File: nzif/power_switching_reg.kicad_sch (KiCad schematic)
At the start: 46 parts, among them U1101 LT8330xS6, U1102 ADP2303ARDZ, U1103 ADP2303ARDZ, U1104 ADP2303ARDZ

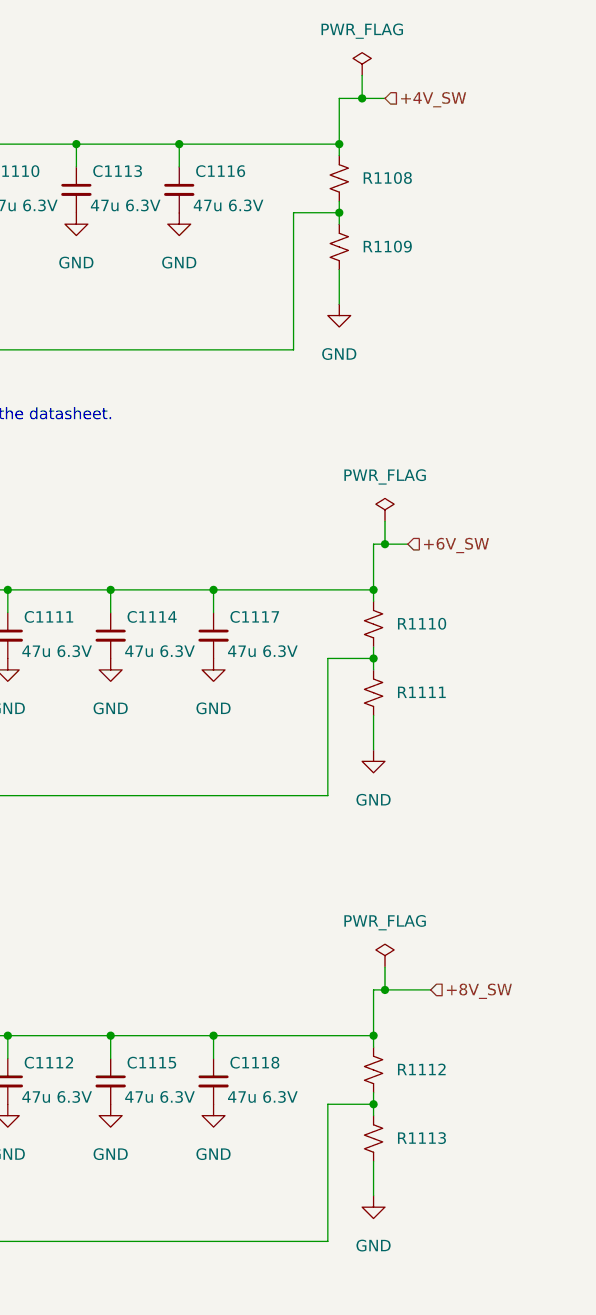
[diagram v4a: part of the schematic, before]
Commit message: updated switching power feedback resistor values
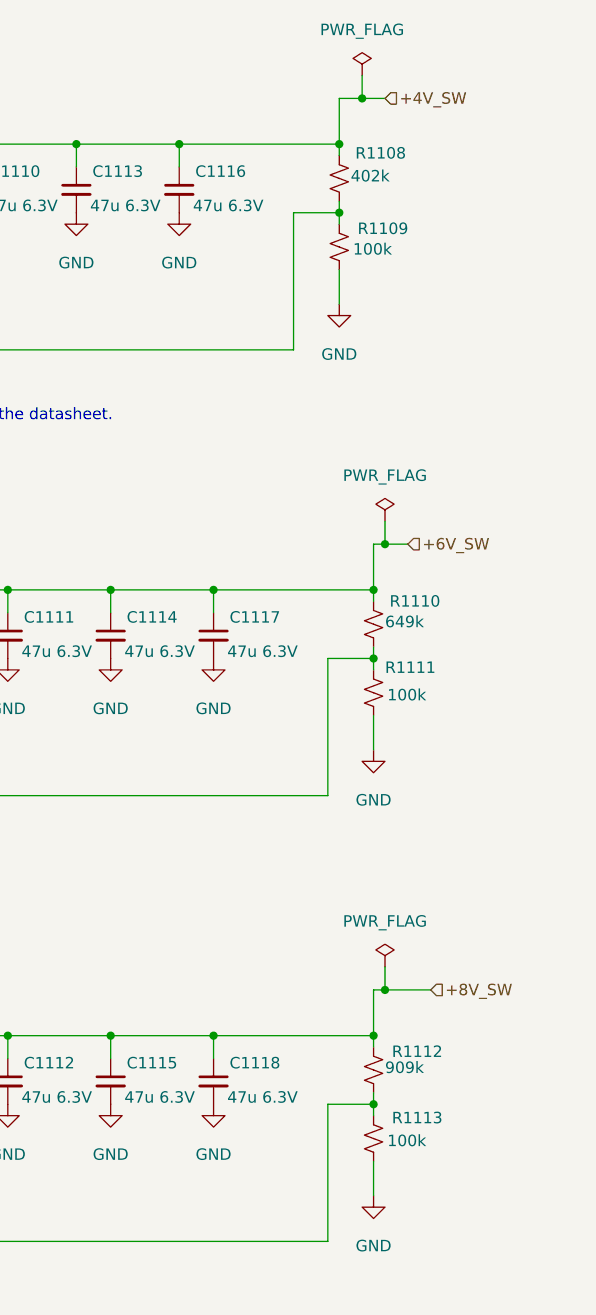
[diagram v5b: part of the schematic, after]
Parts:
- R1108: value (none) -> 402k
- R1109, R1111, R1113: value (none) -> 100k
- R1110: value (none) -> 649k
- R1112: value (none) -> 909k
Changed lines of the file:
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@@
 		(in_pos_files yes)
 		(dnp no)
-		(fields_autoplaced yes)
 		(property "Reference" "R1113"
-			(at 229.87 139.6999 0)
+			(at 229.362 137.414 0)
 			(show_name no)
 			(do_not_autoplace no)
@@
 			)
 		)
-		(property "Value" ""
+		(property "Value" "100k"
 			(at 228.854 139.954 0)
 			(show_name no)
@@
 		(in_pos_files yes)
 		(dnp no)
-		(fields_autoplaced yes)
 		(property "Reference" "R1109"
-			(at 226.06 40.6399 0)
+			(at 225.552 38.608 0)
 			(show_name no)
 			(do_not_autoplace no)
@@
 			)
 		)
-		(property "Value" ""
+		(property "Value" "100k"
 			(at 225.044 40.894 0)
 			(show_name no)
@@
 		(in_pos_files yes)
 		(dnp no)
-		(fields_autoplaced yes)
 		(property "Reference" "R1110"
-			(at 229.87 82.5499 0)
+			(at 229.108 80.01 0)
 			(show_name no)
 			(do_not_autoplace no)
@@
 			)
 		)
-		(property "Value" ""
+		(property "Value" "649k"
 			(at 228.6 82.296 0)
 			(show_name no)
@@
 		(in_pos_files yes)
 		(dnp no)
-		(fields_autoplaced yes)
 		(property "Reference" "R1108"
-			(at 226.06 33.0199 0)
+			(at 225.298 30.226 0)
 			(show_name no)
 			(do_not_autoplace no)
@@
 			)
 		)
-		(property "Value" ""
+		(property "Value" "402k"
 			(at 224.79 32.766 0)
 			(show_name no)
@@
 		(in_pos_files yes)
 		(dnp no)
-		(fields_autoplaced yes)
 		(property "Reference" "R1111"
-			(at 229.87 90.1699 0)
+			(at 228.6 87.376 0)
 			(show_name no)
 			(do_not_autoplace no)
@@
 			)
 		)
-		(property "Value" ""
+		(property "Value" "100k"
 			(at 228.854 90.424 0)
 			(show_name no)
@@
 		(in_pos_files yes)
 		(dnp no)
-		(fields_autoplaced yes)
 		(property "Reference" "R1112"
-			(at 229.87 132.0799 0)
+			(at 229.362 130.048 0)
 			(show_name no)
 			(do_not_autoplace no)
@@
 			)
 		)
-		(property "Value" ""
+		(property "Value" "909k"
 			(at 228.6 131.826 0)
 			(show_name no)
